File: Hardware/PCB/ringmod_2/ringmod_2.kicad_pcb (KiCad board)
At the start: 2 copper layers, 70 x 170 mm, 65 parts, among them J1 Synth_power_2x5, J10 2_pin_Molex_header, J11 2_pin_Molex_header, J2 AudioJack2, J3 AudioJack2, J4 AudioJack2, J5 AudioJack2, J7 3_pin_Molex_header, J8 2_pin_Molex_header, J9 AudioJack2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

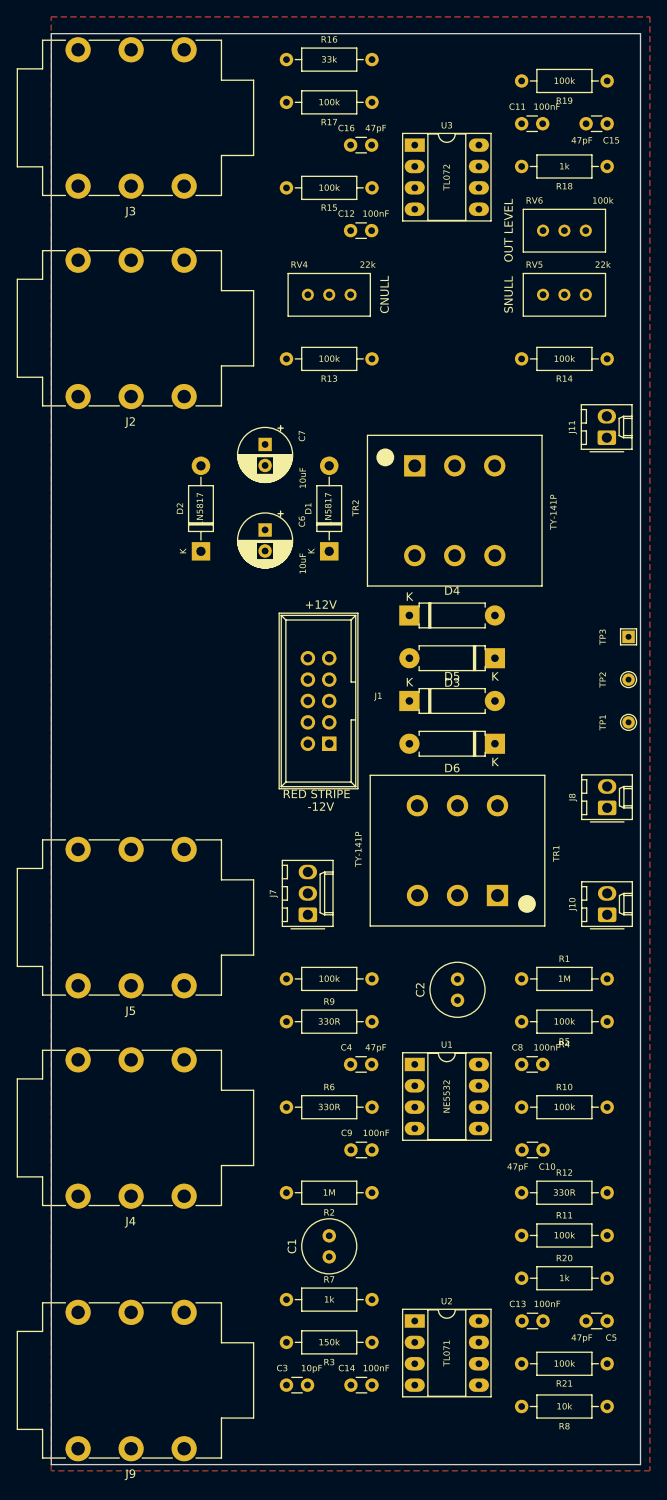
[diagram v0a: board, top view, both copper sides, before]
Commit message: remove inst preamp, redesign panel
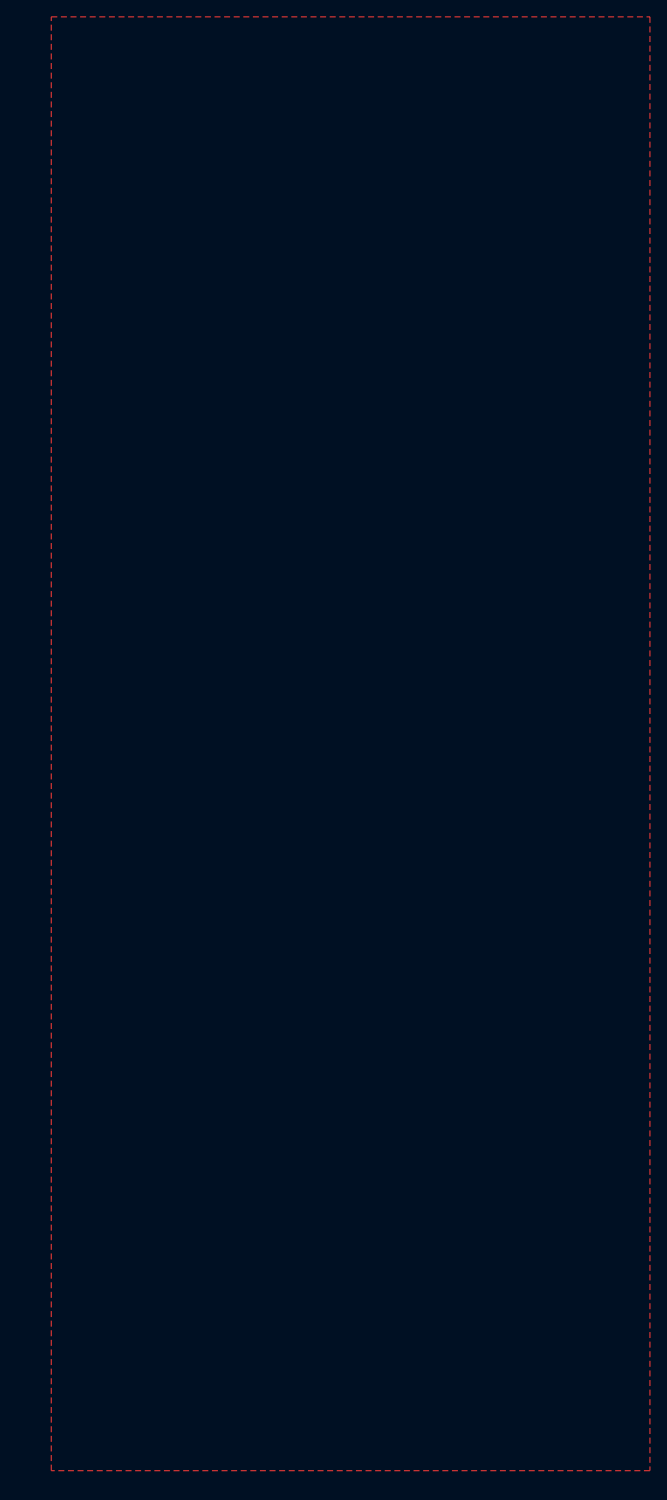
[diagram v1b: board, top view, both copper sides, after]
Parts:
- removed C1, C2: 10uF, Capacitor_THT:C_Radial_D6.3mm_H11.0mm_P2.50mm
- removed C10, C15, C16, C4, C5: 47pF, ao_tht:C_Disc_D3.0mm_W1.6mm_P2.50mm
- removed C11, C12, C13, C14, C8, C9: 100nF, ao_tht:C_Disc_D3.0mm_W1.6mm_P2.50mm
- removed C3: 10pF, ao_tht:C_Disc_D3.0mm_W1.6mm_P2.50mm
- removed C6, C7: 10uF, ao_tht:CP_Radial_D6.3mm_P2.50mm
- removed D1, D2: 1N5817, ao_tht:D_DO-41_SOD81_P10.16mm_Horizontal
- removed D3, D4, D5, D6: 1N695, ringmod:D_DO-7_P10.16mm_Horizontal
- removed J1: Synth_power_2x5, ao_tht:Power_Header
- removed J10, J11, J8: 2_pin_Molex_header, ao_tht:Molex_KK-254_AE-6410-02A_1x02_P2.54mm_Vertical
- removed J2, J3, J4, J5, J9: AudioJack2, ao_tht:Jack_6.35mm_TE-CK-6.35-29B_Horizontal
- removed J7: 3_pin_Molex_header, ao_tht:Molex_KK-254_AE-6410-03A_1x03_P2.54mm_Vertical
- removed R1, R2: 1M, ao_tht:R_Axial_DIN0207_L6.3mm_D2.5mm_P10.16mm_Horizontal
- removed R10, R11, R13, R14, R15, R17, R19, R21, R4, R5: 100k, ao_tht:R_Axial_DIN0207_L6.3mm_D2.5mm_P10.16mm_Horizontal
- removed R12, R6, R9: 330R, ao_tht:R_Axial_DIN0207_L6.3mm_D2.5mm_P10.16mm_Horizontal
- removed R16: 33k, ao_tht:R_Axial_DIN0207_L6.3mm_D2.5mm_P10.16mm_Horizontal
- removed R18, R20, R7: 1k, ao_tht:R_Axial_DIN0207_L6.3mm_D2.5mm_P10.16mm_Horizontal
- removed R3: 150k, ao_tht:R_Axial_DIN0207_L6.3mm_D2.5mm_P10.16mm_Horizontal
- removed R8: 10k, ao_tht:R_Axial_DIN0207_L6.3mm_D2.5mm_P10.16mm_Horizontal
- removed RV4, RV5: 22k, ao_tht:Potentiometer_Bourns_3296W_Vertical_standard
- removed RV6: 100k, ao_tht:Potentiometer_Bourns_3296W_Vertical_standard
- removed TP1: -12V, ao_tht:TestPoint_THTPad_D1.5mm_Drill0.7mm
- removed TP2: +12V, ao_tht:TestPoint_THTPad_D1.5mm_Drill0.7mm
- removed TP3: GND, ao_tht:TestPoint_THTPad_1.5x1.5mm_Drill0.7mm
- removed TR1, TR2: TY-141P, ringmod:Transformer_TY-141P
- removed U1: NE5532, ao_tht:DIP-8_W7.62mm_Socket_LongPads
- removed U2: TL071, ao_tht:DIP-8_W7.62mm_Socket_LongPads
- removed U3: TL072, ao_tht:DIP-8_W7.62mm_Socket_LongPads
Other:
- board outline removed
- board text removed: "CNULL"
- board text removed: "OUT LEVEL"
- board text removed: "SNULL"

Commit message: rm first design; add new holes image
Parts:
- added C1: 47pF, ao_tht:C_Disc_D3.0mm_W1.6mm_P2.50mm, B.Cu at (112.7, 115.2)
- added C10: 100nF, ao_tht:C_Disc_D3.0mm_W1.6mm_P2.50mm, B.Cu at (89.8, 124.1)
- added C11: 100nF, ao_tht:C_Disc_D3.0mm_W1.6mm_P2.50mm, B.Cu at (89.8, 53.0)
- added C2: 47pF, ao_tht:C_Disc_D3.0mm_W1.6mm_P2.50mm, B.Cu at (84.8, 53.0)
- added C3: 10uF, ao_tht:C_Radial_D8.0mm_H11.5mm_P3.50mm, B.Cu at (100.0, 161.0)
- added C4: 47pF, ao_tht:C_Disc_D3.0mm_W1.6mm_P2.50mm, B.Cu at (87.3, 115.2)
- added C5: 47pF, ao_tht:C_Disc_D3.0mm_W1.6mm_P2.50mm, B.Cu at (107.6, 56.8)
- added C6: 10uF, ao_tht:CP_Radial_D6.3mm_P2.50mm, B.Cu at (112.7, 41.6)
- added C7: 100nF, ao_tht:C_Disc_D3.0mm_W1.6mm_P2.50mm, B.Cu at (107.6, 131.8)
- added C8: 100nF, ao_tht:C_Disc_D3.0mm_W1.6mm_P2.50mm, B.Cu at (107.6, 60.6)
- added C9: 10uF, ao_tht:CP_Radial_D6.3mm_P2.50mm, B.Cu at (84.8, 41.6)
- added D1: 1N695, ringmod:D_DO-7_P10.16mm_Horizontal, B.Cu at (87.3, 98.7)
- added D2: 1N695, ringmod:D_DO-7_P10.16mm_Horizontal, B.Cu at (97.5, 93.7)
- added D3: 1N695, ringmod:D_DO-7_P10.16mm_Horizontal, B.Cu at (102.5, 98.7)
- added D4: 1N695, ringmod:D_DO-7_P10.16mm_Horizontal, B.Cu at (112.7, 93.7)
- added D5: 1N5817, ao_tht:D_DO-41_SOD81_P10.16mm_Horizontal, B.Cu at (107.6, 41.6)
- added D6: 1N5817, ao_tht:D_DO-41_SOD81_P10.16mm_Horizontal, B.Cu at (92.4, 31.4)
- added J1: 3_pin_Molex_header, ao_tht:Molex_KK-254_AE-6410-03A_1x03_P2.54mm_Vertical, B.Cu at (119.0, 133.0)
- added J10: AudioJack2, ao_tht:Jack_6.35mm_PJ_629HAN_slots, F.Cu at (112.5, 175.0)
- added J11: Synth_power_2x5, ao_tht:Power_Header, B.Cu at (101.3, 34.0)
- added J3: 2_pin_Molex_header, ao_tht:Molex_KK-254_AE-6410-02A_1x02_P2.54mm_Vertical, B.Cu at (81.0, 117.8)
- added J5: 2_pin_Molex_header, ao_tht:Molex_KK-254_AE-6410-02A_1x02_P2.54mm_Vertical, B.Cu at (119.0, 115.2)
- added J7: AudioJack2, ao_tht:Jack_6.35mm_PJ_629HAN_slots, F.Cu at (112.5, 150.0)
- added J8: AudioJack2, ao_tht:Jack_6.35mm_PJ_629HAN_slots, F.Cu at (87.5, 150.0)
- added J9: AudioJack2, ao_tht:Jack_6.35mm_PJ_629HAN_slots, F.Cu at (87.5, 175.0)
- added R1: 100k, ao_tht:R_Axial_DIN0207_L6.3mm_D2.5mm_P10.16mm_Horizontal, B.Cu at (117.8, 122.9)
- added R10: 330R, ao_tht:R_Axial_DIN0207_L6.3mm_D2.5mm_P10.16mm_Horizontal, B.Cu at (89.8, 127.9)
- added R11: 100k, ao_tht:R_Axial_DIN0207_L6.3mm_D2.5mm_P10.16mm_Horizontal, B.Cu at (86.0, 84.8)
- added R12: 33k, ao_tht:R_Axial_DIN0207_L6.3mm_D2.5mm_P10.16mm_Horizontal, B.Cu at (107.6, 64.4)
- added R13: 1k, ao_tht:R_Axial_DIN0207_L6.3mm_D2.5mm_P10.16mm_Horizontal, B.Cu at (107.6, 47.9)
- added R14: 100k, ao_tht:R_Axial_DIN0207_L6.3mm_D2.5mm_P10.16mm_Horizontal, B.Cu at (117.8, 51.7)
- added R2: 330R, ao_tht:R_Axial_DIN0207_L6.3mm_D2.5mm_P10.16mm_Horizontal, B.Cu at (107.6, 127.9)
- added R3: 100k, ao_tht:R_Axial_DIN0207_L6.3mm_D2.5mm_P10.16mm_Horizontal, B.Cu at (105.1, 64.4)
- added R4: 100k, ao_tht:R_Axial_DIN0207_L6.3mm_D2.5mm_P10.16mm_Horizontal, B.Cu at (79.7, 138.1)
- added R5: 100k, ao_tht:R_Axial_DIN0207_L6.3mm_D2.5mm_P10.16mm_Horizontal, B.Cu at (92.4, 56.8)
- added R6: 100k, ao_tht:R_Axial_DIN0207_L6.3mm_D2.5mm_P10.16mm_Horizontal, B.Cu at (81.0, 84.8)
- added R7: 100k, ao_tht:R_Axial_DIN0207_L6.3mm_D2.5mm_P10.16mm_Horizontal, B.Cu at (100.0, 154.6)
- added R8: 1M, ao_tht:R_Axial_DIN0207_L6.3mm_D2.5mm_P10.16mm_Horizontal, B.Cu at (89.8, 162.2)
- added R9: 330R, ao_tht:R_Axial_DIN0207_L6.3mm_D2.5mm_P10.16mm_Horizontal, B.Cu at (89.8, 133.0)
- added RV7: 20k, ao_tht:Potentiometer_Bourns_3296W_Vertical_standard, B.Cu at (91.1, 68.2)
- added RV8: 20k, ao_tht:Potentiometer_Bourns_3296W_Vertical_standard, B.Cu at (91.1, 61.9)
- added RV9: 100k, ao_tht:Potentiometer_Bourns_3296W_Vertical_standard, B.Cu at (115.2, 56.8)
- added TP1: -12V, ao_tht:TestPoint_THTPad_D1.5mm_Drill0.7mm, B.Cu at (79.7, 46.7)
- added TP2: +12V, ao_tht:TestPoint_THTPad_D1.5mm_Drill0.7mm, B.Cu at (79.7, 31.4)
- added TP3: GND, ao_tht:TestPoint_THTPad_1.5x1.5mm_Drill0.7mm, B.Cu at (79.7, 39.0)
- added TR1: TY-141P, ringmod:Transformer_TY-141P, B.Cu at (95.2, 115.5)
- added TR2: TY-141P, ringmod:Transformer_TY-141P, B.Cu at (104.7, 76.6)
- added U1: NE5532, ao_tht:DIP-8_W7.62mm_Socket_LongPads, B.Cu at (96.2, 131.8)
- added U2: TL072, ao_tht:DIP-8_W7.62mm_Socket_LongPads, B.Cu at (96.2, 60.6)
- GRAF1: footprint ringmod_panel:ringmod_panel_2_holes -> ringmod:ringmod_panel_2_holes
- moved GRAF1 14.1 mm to (100.0, 100.0)
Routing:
- net +12V: track 0.00 -> 158.0 mm
- net /Main PCB/OUT: track 0.00 -> 129.0 mm
- net -12V: track 0.00 -> 109.8 mm
- net /Main PCB/SIGLVL_CW: track 0.00 -> 78.2 mm
- net /Main PCB/CARRLVL_CW: track 0.00 -> 61.8 mm
- net /Main PCB/CARRLVL_CCW: track 0.00 -> 59.7 mm
- net Net-(C5-Pad1): track 0.00 -> 43.2 mm
- net Net-(C2-Pad1): track 0.00 -> 34.0 mm
- net Net-(C2-Pad2): track 0.00 -> 32.4 mm
- net /Main PCB/UNBAL_WIP: track 0.00 -> 30.3 mm
- net /Main PCB/SIG IN: track 0.00 -> 27.5 mm
- net /Main PCB/SIGLVL_CCW: track 0.00 -> 21.5 mm
- net Net-(C4-Pad2): track 0.00 -> 19.2 mm
- net /Main PCB/AC CARR IN: track 0.00 -> 18.6 mm
- net /Main PCB/+12_IN: track 0.00 -> 17.9 mm
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- added copper zone on B.Cu, net GND
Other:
- board outline added: 46 x 160 mm

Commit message: Layout revision
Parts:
- moved C3 26.9 mm to (108.9, 135.6), turned to 0 degrees
- moved R8 21.6 mm to (100.0, 143.2), turned to -90 degrees
- moved J1 20.3 mm to (119.0, 112.7)
- moved R7 19.4 mm to (89.8, 138.1), turned to 180 degrees
- moved J5 11.4 mm to (119.0, 103.8)
- moved R9 5.08 mm to (89.8, 127.9)
- moved R10 5.08 mm to (89.8, 122.9)
- moved R4 5.08 mm to (79.7, 133.0)
- moved C10 3.59 mm to (92.4, 126.7), turned to 90 degrees
- moved C7 2.54 mm to (107.6, 129.2), turned to 90 degrees
- moved R1 2.54 mm to (120.3, 122.9)
- moved R2 2.54 mm to (110.2, 127.9)
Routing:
- net /Main PCB/AC CARR IN: track 18.6 -> 46.4 mm
- net /Main PCB/SIGLVL_CW: track 78.2 -> 93.4 mm
- net Net-(C3-Pad1): track 6.35 -> 20.1 mm
- net /Main PCB/CARRLVL_CCW: track 59.7 -> 46.4 mm
- net /Main PCB/SIGLVL_CCW: track 21.5 -> 30.7 mm
- net /Main PCB/DC CARR IN: track 9.60 -> 15.4 mm
- net +12V: track 158.0 -> 163.2 mm
- net /Main PCB/CARRLVL_CW: track 61.8 -> 56.7 mm
- net /Main PCB/UNBAL_WIP: track 30.3 -> 34.5 mm
- net /Main PCB/SIG IN: track 27.5 -> 24.2 mm
- net Net-(C1-Pad2): track 16.6 -> 18.1 mm
- net Net-(C4-Pad2): track 19.2 -> 17.9 mm
- net /Main PCB/OUT: track 129.0 -> 130.1 mm
